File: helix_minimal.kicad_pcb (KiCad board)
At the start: 2 copper layers, 50 x 50 mm, 20 parts, among them J1 USB-C, J4 sd card, J5 SWD, J6 pico hdmi, U1 STM32C071FBP6, U2 AP2112K-3.3, U3 WIZ850io

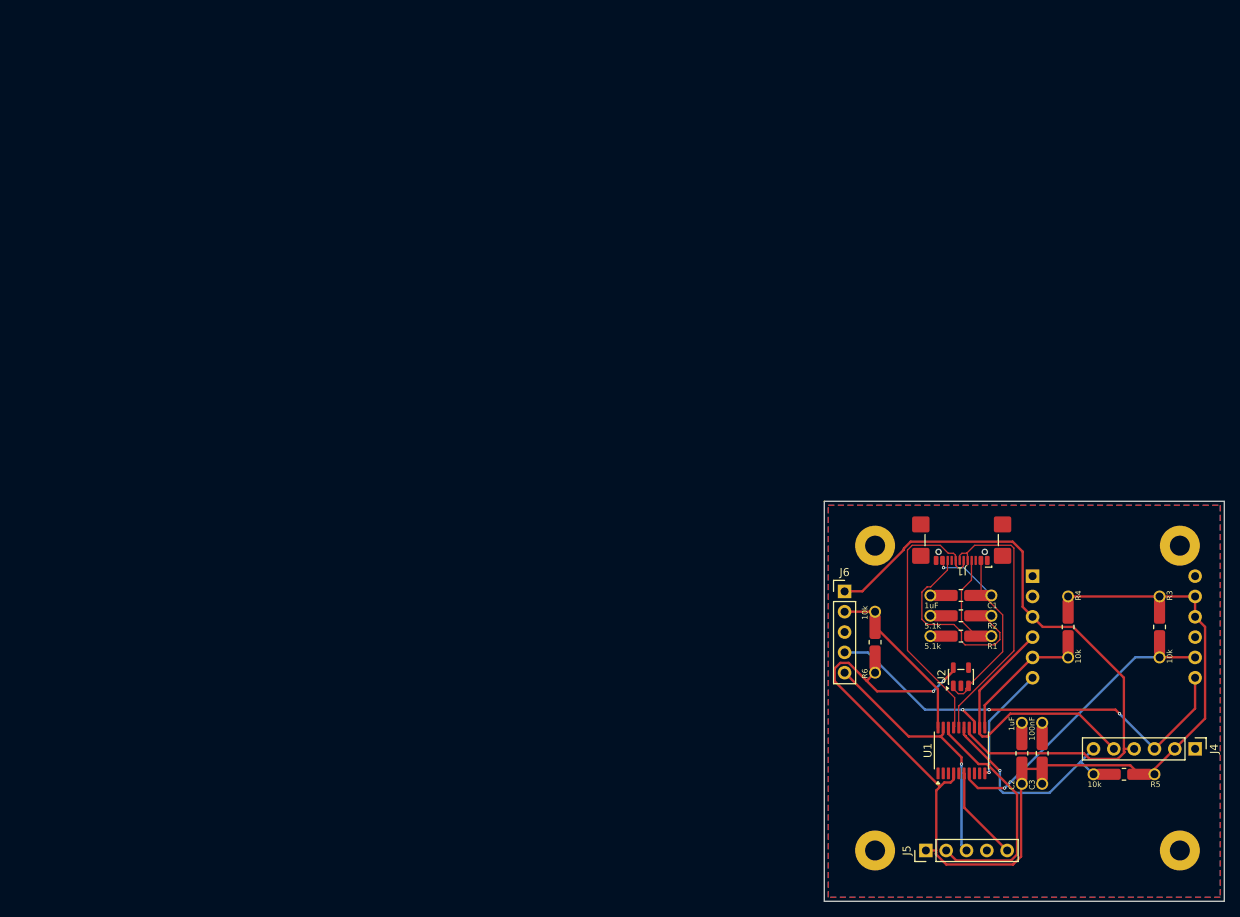
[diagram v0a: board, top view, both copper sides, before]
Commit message: Clear copper and preserve manual USB data routes
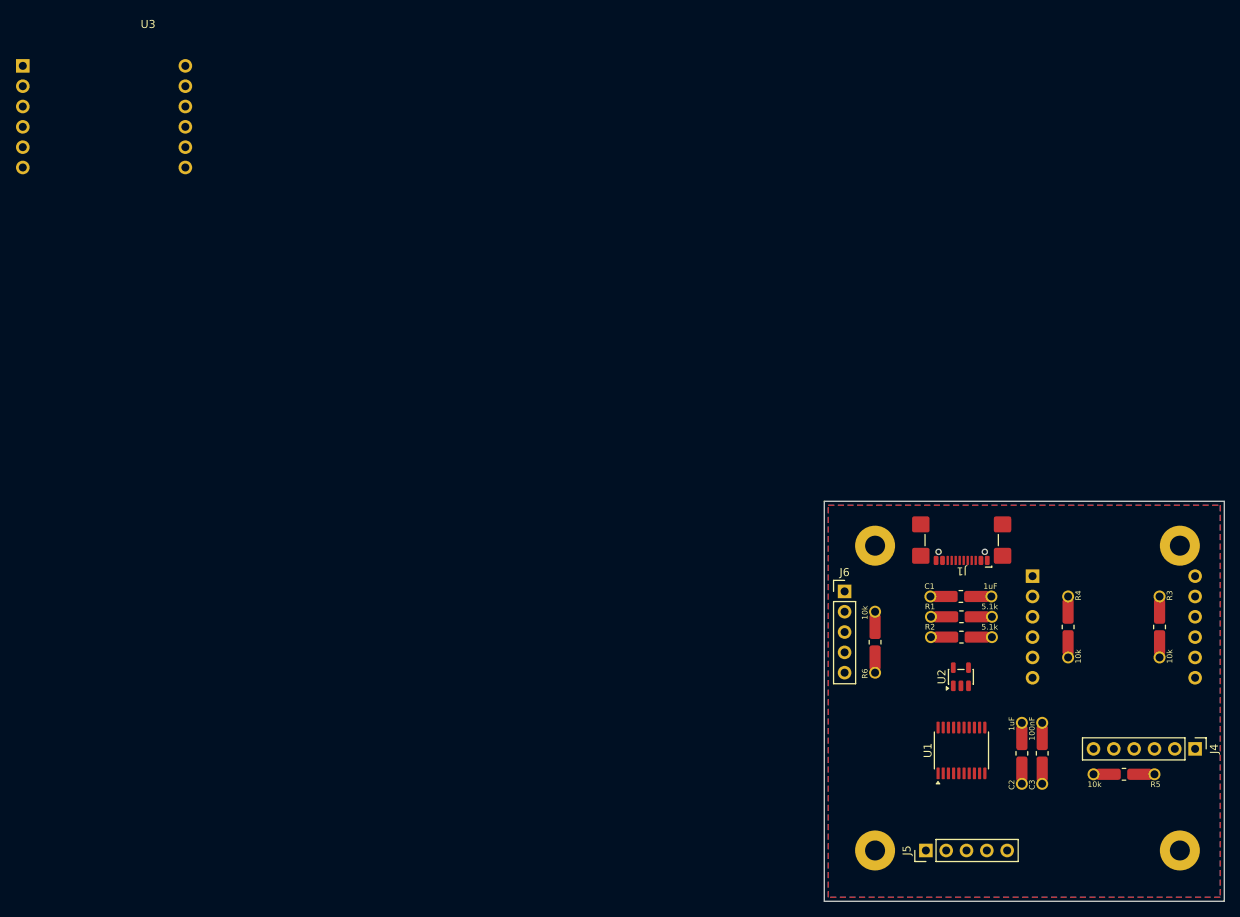
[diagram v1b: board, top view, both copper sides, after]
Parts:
- added U3: WIZ850io, Helix:WIZ850io, F.Cu at (11.6, 9.88)
- moved R2 2.67 mm to (118.7, 81.3), turned to 0 degrees
- moved R1 2.41 mm to (118.7, 78.7), turned to 0 degrees
- moved C1 0.13 mm to (118.7, 76.2), turned to 0 degrees
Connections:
- C1 pad 1: VBUS -> GND
- C1 pad 2: GND -> VBUS
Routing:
- net +3V3: track 131.7 -> 0.00 mm, vias 2 -> 0
- net /SPI_MOSI: track 81.1 -> 0.00 mm
- net /SPI_MISO: track 57.6 -> 0.00 mm, vias 3 -> 0
- net /WIZ_RST: track 35.5 -> 0.00 mm, vias 1 -> 0
- net /SPI_SCK: track 34.8 -> 0.00 mm
- net /USB_DP: track 34.7 -> 0.00 mm
- net /USB_DM: track 33.8 -> 0.00 mm
- net /SWCLK: track 32.2 -> 0.00 mm, vias 1 -> 0
- net VBUS: track 31.1 -> 0.00 mm, vias 1 -> 0
- net /SWDIO: track 29.7 -> 0.00 mm
- net /SD_CS: track 26.0 -> 0.00 mm, vias 1 -> 0
- net /CC2: track 25.7 -> 0.00 mm
- net /PICO_CS: track 19.7 -> 0.00 mm
- net /WIZ_CS: track 15.7 -> 0.00 mm
- net /WIZ_INT: track 14.7 -> 0.00 mm, vias 1 -> 0
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
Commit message: Route around manual USB data pair and preserve schematic edits
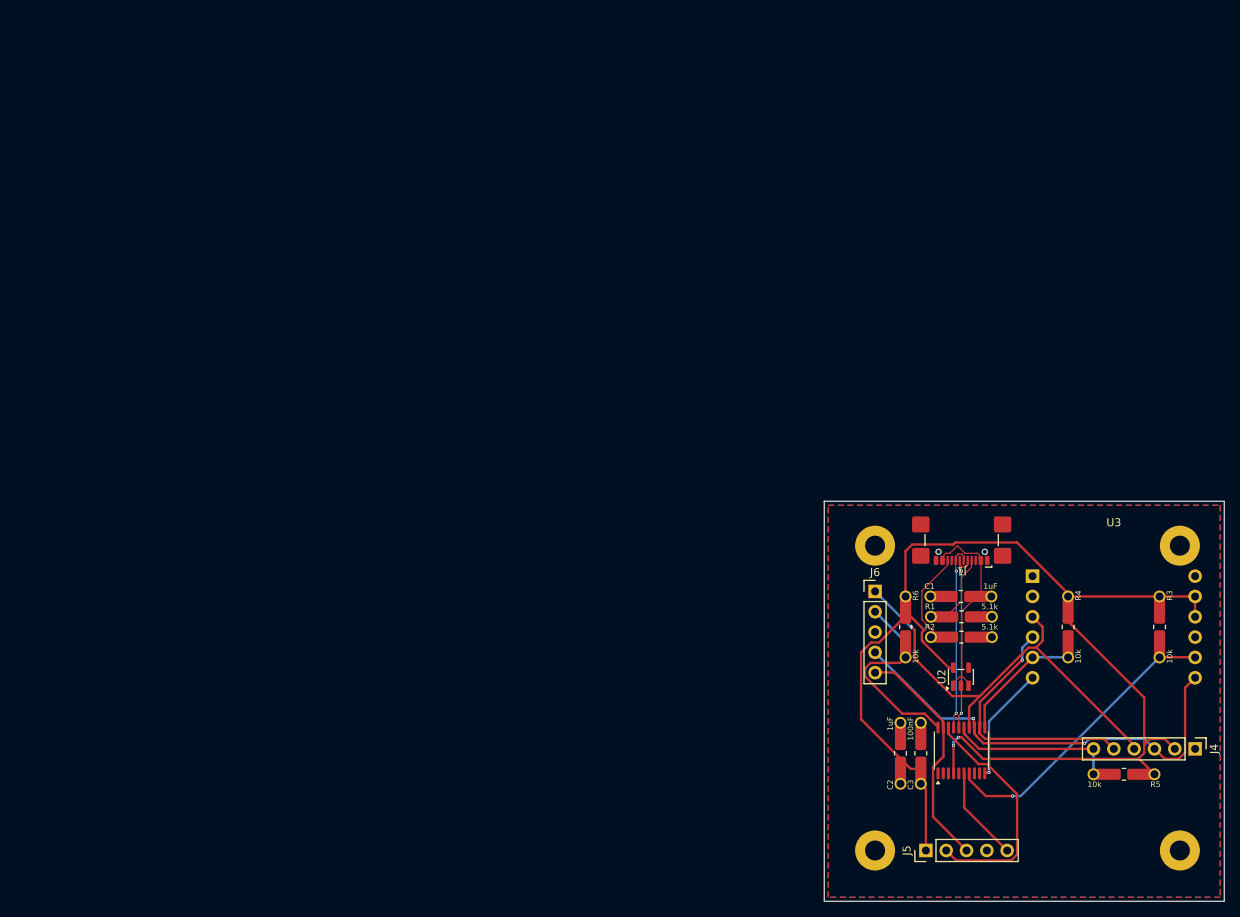
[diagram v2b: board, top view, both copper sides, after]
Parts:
- removed the U3 at (137.8, 73.7)
- moved U3 141.4 mm to (137.8, 73.7)
- moved C2 15.2 mm to (111.1, 95.8)
- moved C3 15.2 mm to (113.7, 95.8)
- moved R6 4.26 mm to (111.8, 80.0), turned to -90 degrees
- moved J6 3.81 mm to (108.0, 75.6)
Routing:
- net +3V3: track 0.00 -> 153.8 mm, vias 0 -> 2
- net /SPI_MOSI: track 0.00 -> 57.0 mm, vias 0 -> 1
- net /SPI_MISO: track 0.00 -> 55.9 mm, vias 0 -> 2
- net /WIZ_RST: track 0.00 -> 36.3 mm, vias 0 -> 1
- net /SPI_SCK: track 0.00 -> 32.4 mm, vias 0 -> 1
- net /SWDIO: track 0.00 -> 29.7 mm
- net /SWCLK: track 0.00 -> 29.5 mm
- net VBUS: track 0.00 -> 25.8 mm
- net /PICO_CS: track 0.00 -> 25.7 mm
- net /USB_DM: track 0.00 -> 23.5 mm, vias 0 -> 2
- net /USB_DP: track 0.00 -> 23.4 mm, vias 0 -> 2
- net /SD_CS: track 0.00 -> 20.9 mm
- net /WIZ_CS: track 0.00 -> 15.7 mm
- net /WIZ_INT: track 0.00 -> 14.7 mm, vias 0 -> 1
- net /CC2: track 0.00 -> 12.7 mm
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
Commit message: Reroute signals with stronger layer direction preference and quadratic route selection
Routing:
- net +3V3: track 153.8 -> 117.0 mm
- net /WIZ_RST: track 36.3 -> 40.7 mm, vias 1 -> 2
- net /SPI_MISO: track 55.9 -> 52.5 mm
- net /SPI_MOSI: track 57.0 -> 60.3 mm, vias 1 -> 0
- net /PICO_CS: track 25.7 -> 23.8 mm
- net /SPI_SCK: vias 1 -> 0
